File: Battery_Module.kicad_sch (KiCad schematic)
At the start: 7 parts, among them Q701 FS8205A, U701 DW01A

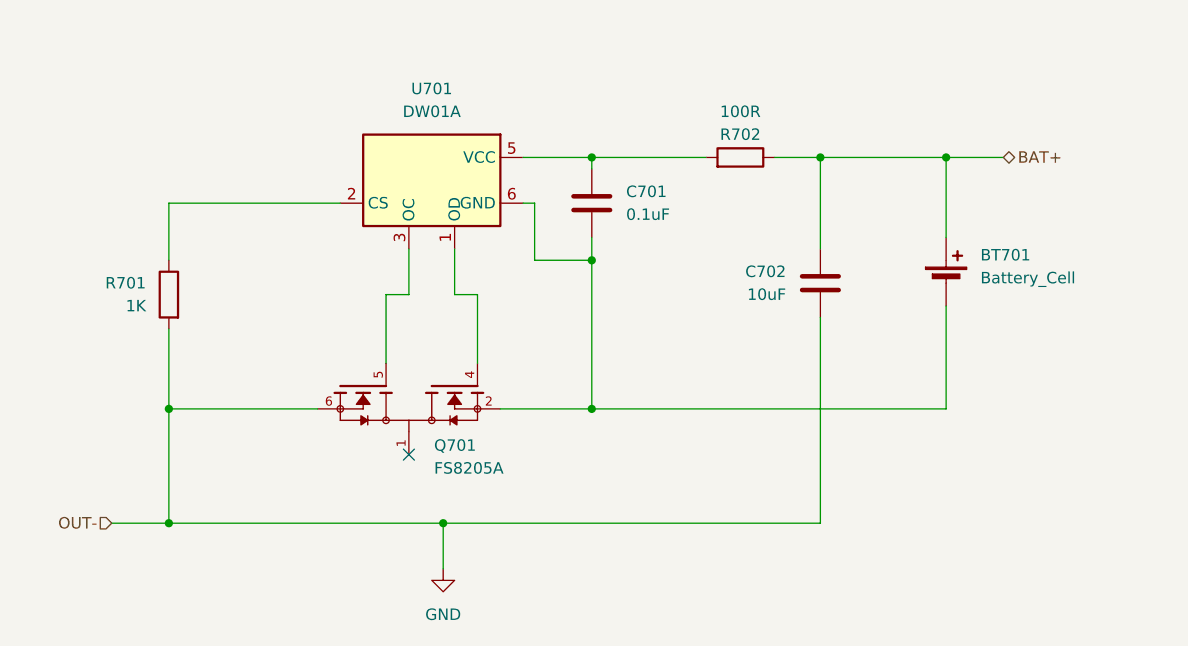
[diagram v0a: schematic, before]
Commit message: "3.3V buck boost converter added. few footprints added"
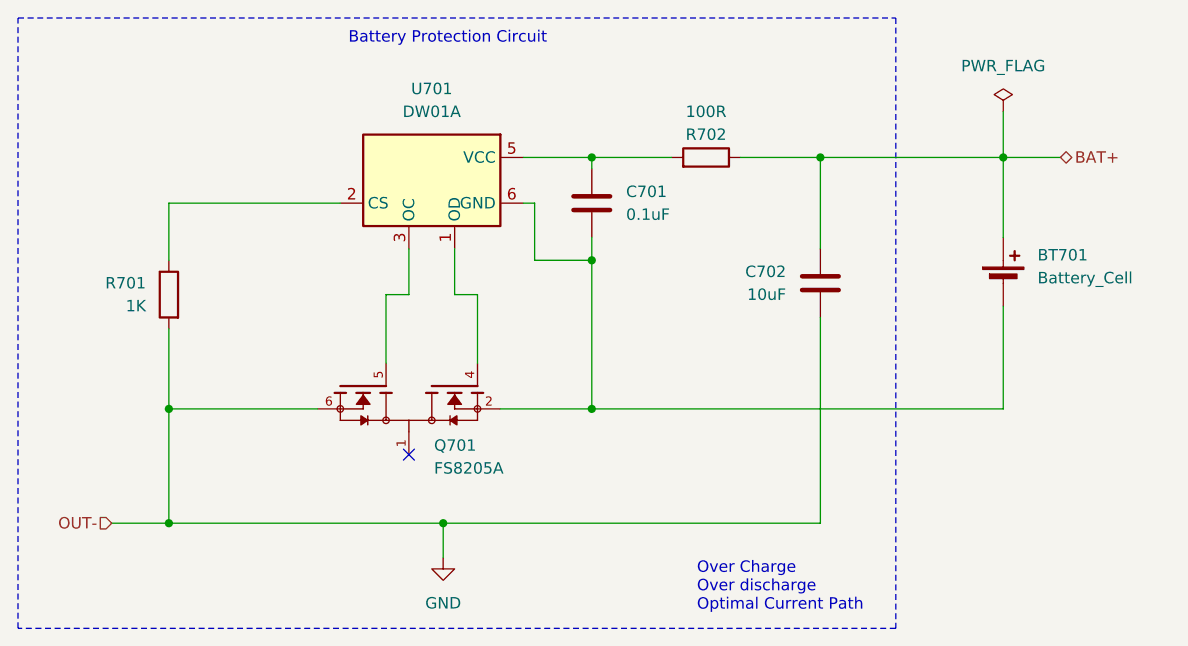
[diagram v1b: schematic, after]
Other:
- note added: "Battery Protection Circuit"
- note added: "Over Charge Over discharge Optimal Current Path"
- moved on the sheet: BT701, R702
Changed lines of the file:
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@@
 	(generator_version "9.0")
 	(paper "A4")
+	(rectangle
+		(start 83.566 72.136)
+		(end 181.102 139.954)
+		(stroke
+			(width 0)
+			(type dash)
+		)
+		(fill
+			(type none)
+		)
+	)
+	(text "Over Charge\nOver discharge\nOptimal Current Path"
+		(exclude_from_sim no)
+		(at 159.004 135.382 0)
+		(effects
+			(font
+				(size 1.27 1.27)
+			)
+			(justify left)
+		)
+	)
+	(text "Battery Protection Circuit"
+		(exclude_from_sim no)
+		(at 131.318 74.422 0)
+		(effects
+			(font
+				(size 1.27 1.27)
+			)
+		)
+	)
 	(junction
 		(at 172.72 87.63)
@@
 	)
 	(junction
-		(at 186.69 87.63)
+		(at 193.04 87.63)
 		(diameter 0)
 		(color 0 0 0 0)
@@
 	(wire
 		(pts
-			(xy 167.64 87.63) (xy 172.72 87.63)
+			(xy 163.83 87.63) (xy 172.72 87.63)
 		)
 		(stroke
@@
 	(wire
 		(pts
-			(xy 186.69 87.63) (xy 186.69 96.52)
+			(xy 193.04 87.63) (xy 193.04 96.52)
 		)
 		(stroke
@@
 	(wire
 		(pts
-			(xy 172.72 87.63) (xy 186.69 87.63)
-		)
-		(stroke
-			(width 0)
-			(type default)
-		)
-	)
-	(wire
-		(pts
-			(xy 130.81 128.27) (xy 130.81 133.35)
+			(xy 172.72 87.63) (xy 193.04 87.63)
+		)
+		(stroke
+			(width 0)
+			(type default)
+		)
+	)
+	(wire
+		(pts
+			(xy 130.81 128.27) (xy 130.81 132.08)
 		)
 		(stroke
@@
 	(wire
 		(pts
+			(xy 193.04 82.55) (xy 193.04 87.63)
+		)
+		(stroke
+			(width 0)
+			(type default)
+		)
+	)
+	(wire
+		(pts
 			(xy 127 97.79) (xy 127 102.87)
 		)
@@
 	(wire
 		(pts
-			(xy 160.02 87.63) (xy 147.32 87.63)
-		)
-		(stroke
-			(width 0)
-			(type default)
-		)
-	)
-	(wire
-		(pts
-			(xy 186.69 87.63) (xy 193.04 87.63)
-		)
-		(stroke
-			(width 0)
-			(type default)
-		)
-	)
-	(wire
-		(pts
-			(xy 147.32 115.57) (xy 186.69 115.57)
+			(xy 156.21 87.63) (xy 147.32 87.63)
+		)
+		(stroke
+			(width 0)
+			(type default)
+		)
+	)
+	(wire
+		(pts
+			(xy 193.04 87.63) (xy 199.39 87.63)
+		)
+		(stroke
+			(width 0)
+			(type default)
+		)
+	)
+	(wire
+		(pts
+			(xy 147.32 115.57) (xy 193.04 115.57)
 		)
 		(stroke
@@
 	(wire
 		(pts
-			(xy 186.69 104.14) (xy 186.69 115.57)
+			(xy 193.04 104.14) (xy 193.04 115.57)
 		)
 		(stroke
@@
 	(hierarchical_label "BAT+"
 		(shape bidirectional)
-		(at 193.04 87.63 0)
+		(at 199.39 87.63 0)
 		(effects
 			(font
@@
 	(symbol
 		(lib_id "Device:R")
-		(at 163.83 87.63 270)
+		(at 160.02 87.63 270)
 		(mirror x)
 		(unit 1)
@@
 		(dnp no)
 		(property "Reference" "R702"
-			(at 163.83 85.09 90)
+			(at 160.02 85.09 90)
 			(effects
 				(font
@@
 		)
 		(property "Value" "100R"
-			(at 163.83 82.55 90)
+			(at 160.02 82.55 90)
 			(effects
 				(font
@@
 		)
 		(property "Footprint" ""
-			(at 163.83 89.408 90)
+			(at 160.02 89.408 90)
 			(effects
 				(font
@@
 		)
 		(property "Datasheet" "~"
-			(at 163.83 87.63 0)
+			(at 160.02 87.63 0)
 			(effects
 				(font
@@
 		)
 		(property "Description" "Resistor"
-			(at 163.83 87.63 0)
+			(at 160.02 87.63 0)
 			(effects
 				(font
@@
 	(symbol
 		(lib_id "power:GND")
-		(at 130.81 133.35 0)
+		(at 130.81 132.08 0)
 		(unit 1)
 		(exclude_from_sim no)
@@
 		(fields_autoplaced yes)
 		(property "Reference" "#PWR0702"
-			(at 130.81 139.7 0)
+			(at 130.81 138.43 0)
 			(effects
 				(font
@@
 		)
 		(property "Value" "GND"
-			(at 130.81 138.43 0)
+			(at 130.81 137.16 0)
 			(effects
 				(font
@@
 		)
 		(property "Footprint" ""
-			(at 130.81 133.35 0)
+			(at 130.81 132.08 0)
 			(effects
 				(font
@@
 		)
 		(property "Datasheet" ""
-			(at 130.81 133.35 0)
+			(at 130.81 132.08 0)
 			(effects
 				(font
@@
 		)
 		(property "Description" "Power symbol creates a global label with name \"GND\" , ground"
-			(at 130.81 133.35 0)
+			(at 130.81 132.08 0)
 			(effects
 				(font
@@
 	(symbol
 		(lib_id "Device:Battery_Cell")
-		(at 186.69 101.6 0)
+		(at 193.04 101.6 0)
 		(unit 1)
 		(exclude_from_sim no)
@@
 		(fields_autoplaced yes)
 		(property "Reference" "BT701"
-			(at 190.5 98.4884 0)
+			(at 196.85 98.4884 0)
 			(effects
 				(font
@@
 		)
 		(property "Value" "Battery_Cell"
-			(at 190.5 101.0284 0)
+			(at 196.85 101.0284 0)
 			(effects
 				(font
@@
 		)
 		(property "Footprint" "govi_v3_SHT41_sensor_kicad:BAT_1042P"
-			(at 186.69 100.076 90)
+			(at 193.04 100.076 90)
 			(effects
 				(font
@@
 		)
 		(property "Datasheet" "~"
-			(at 186.69 100.076 90)
+			(at 193.04 100.076 90)
 			(effects
 				(font
@@
 		)
 		(property "Description" "Single-cell battery"
-			(at 186.69 101.6 0)
+			(at 193.04 101.6 0)
 			(effects
 				(font
@@
 					(unit 1)
 				)
+			)
+		)
+	)
+	(symbol
+		(lib_id "power:PWR_FLAG")
+		(at 193.04 82.55 0)
+		(unit 1)
+		(exclude_from_sim no)
+		(in_bom yes)
+		(on_board yes)
+		(dnp no)
+		(fields_autoplaced yes)
+		(property "Reference" "#FLG0701"
+			(at 193.04 80.645 0)
+			(effects
+				(font
+					(size 1.27 1.27)
+				)
+				(hide yes)
+			)
+		)
+		(property "Value" "PWR_FLAG"
+			(at 193.04 77.47 0)
+			(effects
+				(font
+					(size 1.27 1.27)
+				)
+			)
+		)
+		(property "Footprint" ""
+			(at 193.04 82.55 0)
+			(effects
+				(font
+					(size 1.27 1.27)
+				)
+				(hide yes)
+			)
+		)
+		(property "Datasheet" "~"
+			(at 193.04 82.55 0)
+			(effects
+				(font
+					(size 1.27 1.27)
+				)
+				(hide yes)
+			)
+		)
+		(property "Description" "Special symbol for telling ERC where power comes from"
+			(at 193.04 82.55 0)
+			(effects
+				(font
+					(size 1.27 1.27)
+				)
+				(hide yes)
+			)
+		)
+		(pin "1"
+		)
+		(instances
+			(project "govi_v3_SHT41_sensor_kicad"
+				(path "/ba95ddf4-72c6-4eeb-9c09-ae7c8e5af670/625f4f9c-da9a-4f02-8306-7d03107693c0"
+					(reference "#FLG0701")
+					(unit 1)
+				)

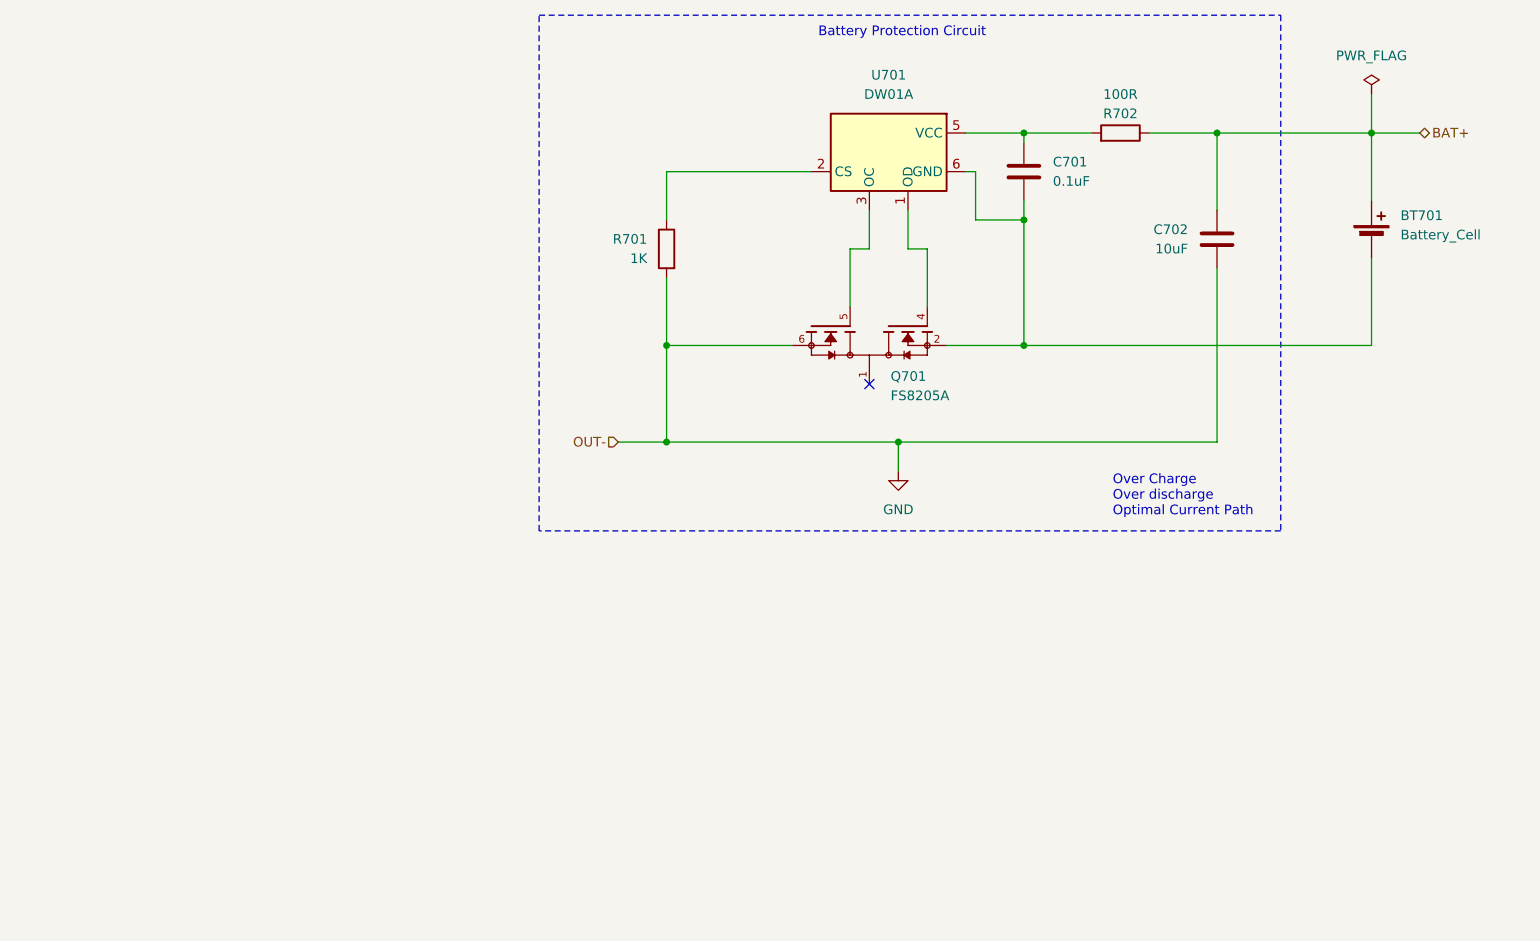
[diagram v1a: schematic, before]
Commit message: "Assign Footprints Done"
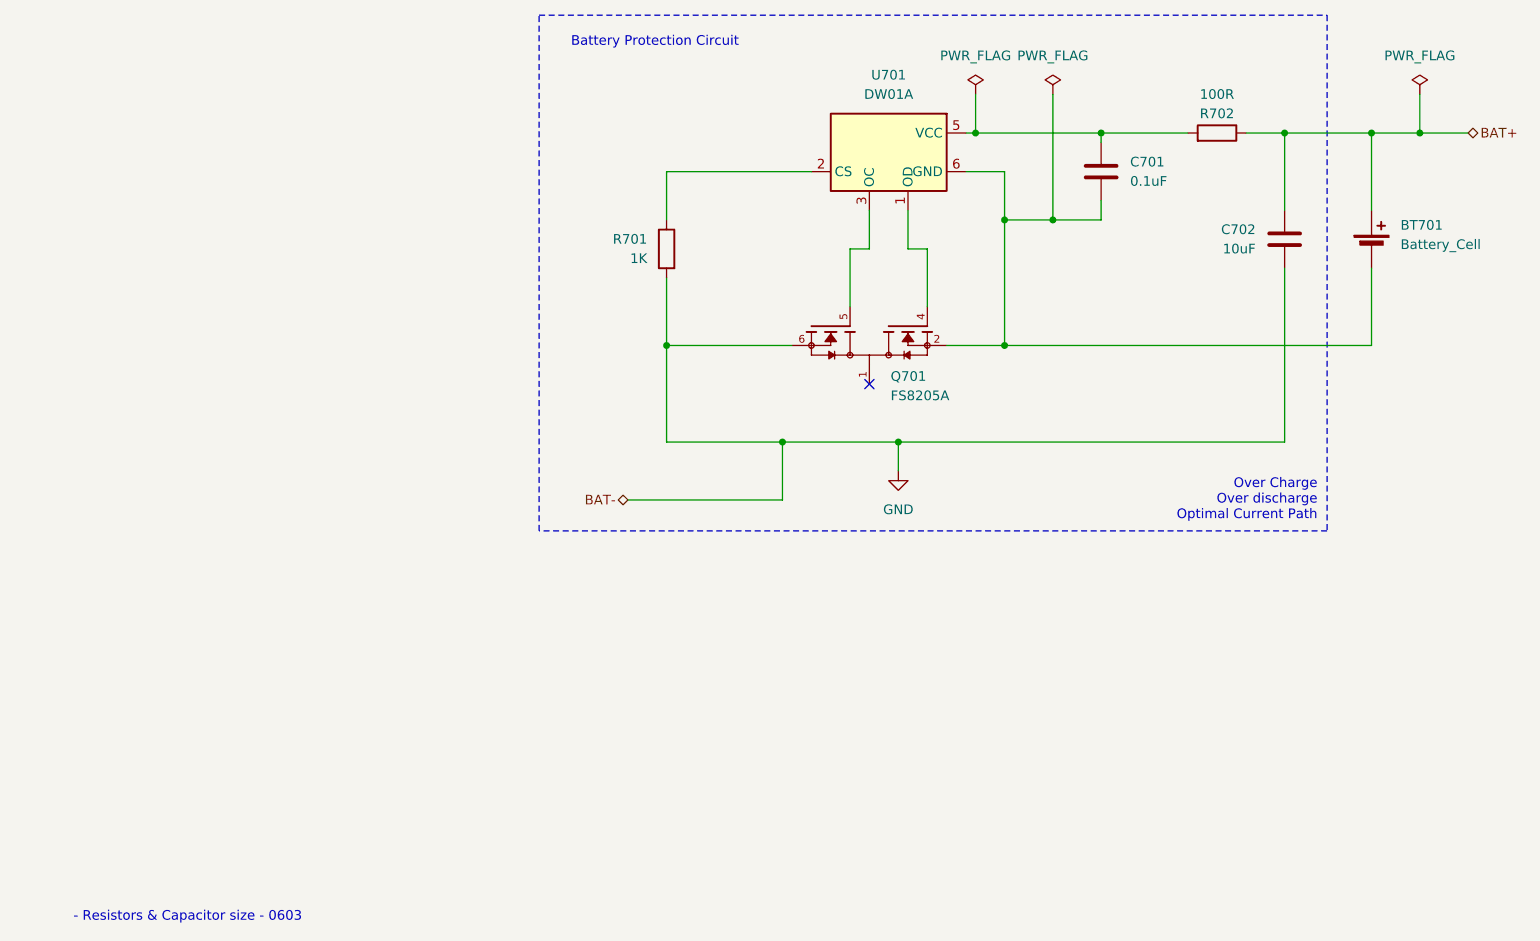
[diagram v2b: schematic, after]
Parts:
- C701, C702: footprint (none) -> Capacitor_SMD:C_0603_1608Metric_Pad1.08x0.95mm_HandSolder
- R701, R702: footprint (none) -> Resistor_SMD:R_0603_1608Metric_Pad0.98x0.95mm_HandSolder
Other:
- note added: "- Resistors & Capacitor size - 0603"
- moved on the sheet: BT701, C701, C702, R702

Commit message: "PCB front Layer Component assembly done"
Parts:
- added TP701: BAT-, TestPoint:TestPoint_Pad_D1.0mm, symbol Connector:TestPoint
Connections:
- net GND: now also TP701.1
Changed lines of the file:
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@@
+	)
+	(junction
+		(at 104.14 115.57)
+		(diameter 0)
+		(color 0 0 0 0)
 	)
 	(junction
@@
 	(wire
 		(pts
+			(xy 104.14 115.57) (xy 116.84 115.57)
+		)
+		(stroke
+			(width 0)
+			(type default)
+		)
+	)
+	(wire
+		(pts
 			(xy 132.08 102.87) (xy 134.62 102.87)
 		)
@@
 	(wire
 		(pts
+			(xy 104.14 114.3) (xy 104.14 115.57)
+		)
+		(stroke
+			(width 0)
+			(type default)
+		)
+	)
+	(wire
+		(pts
 			(xy 140.97 87.63) (xy 157.48 87.63)
 		)
@@
 	(wire
 		(pts
-			(xy 100.33 115.57) (xy 116.84 115.57)
+			(xy 100.33 115.57) (xy 104.14 115.57)
 		)
 		(stroke
@@
 					(unit 1)
 				)
+			)
+		)
+	)
+	(symbol
+		(lib_id "Connector:TestPoint")
+		(at 104.14 114.3 0)
+		(unit 1)
+		(exclude_from_sim no)
+		(in_bom yes)
+		(on_board yes)
+		(dnp no)
+		(fields_autoplaced yes)
+		(property "Reference" "TP701"
+			(at 106.68 109.7279 0)
+			(effects
+				(font
+					(size 1.27 1.27)
+				)
+				(justify left)
+			)
+		)
+		(property "Value" "BAT-"
+			(at 106.68 112.2679 0)
+			(effects
+				(font
+					(size 1.27 1.27)
+				)
+				(justify left)
+			)
+		)
+		(property "Footprint" "TestPoint:TestPoint_Pad_D1.0mm"
+			(at 109.22 114.3 0)
+			(effects
+				(font
+					(size 1.27 1.27)
+				)
+				(hide yes)
+			)
+		)
+		(property "Datasheet" "~"
+			(at 109.22 114.3 0)
+			(effects
+				(font
+					(size 1.27 1.27)
+				)
+				(hide yes)
+			)
+		)
+		(property "Description" "test point"
+			(at 104.14 114.3 0)
+			(effects
+				(font
+					(size 1.27 1.27)
+				)
+				(hide yes)
+			)
+		)
+		(pin "1"
+		)
+		(instances
+			(project ""
+				(path "/ba95ddf4-72c6-4eeb-9c09-ae7c8e5af670/625f4f9c-da9a-4f02-8306-7d03107693c0"
+					(reference "TP701")
+					(unit 1)
+				)

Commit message: "Before changing the orientation of the LoRa module. removing existing LoRa module routing."
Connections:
- net GND renamed BAT-
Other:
- moved on the sheet: TP701
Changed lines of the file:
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@@
+	)
+	(junction
+		(at 110.49 115.57)
+		(diameter 0)
+		(color 0 0 0 0)
 	)
 	(junction
@@
 	)
 	(junction
-		(at 104.14 115.57)
-		(diameter 0)
-		(color 0 0 0 0)
-	)
-	(junction
 		(at 140.97 87.63)
 		(diameter 0)
@@
 	(junction
 		(at 181.61 87.63)
-		(diameter 0)
-		(color 0 0 0 0)
-	)
-	(junction
-		(at 130.81 128.27)
 		(diameter 0)
 		(color 0 0 0 0)
@@
 	(wire
 		(pts
-			(xy 104.14 115.57) (xy 116.84 115.57)
+			(xy 110.49 110.49) (xy 110.49 115.57)
 		)
 		(stroke
@@
 	(wire
 		(pts
-			(xy 130.81 128.27) (xy 181.61 128.27)
-		)
-		(stroke
-			(width 0)
-			(type default)
-		)
-	)
-	(wire
-		(pts
-			(xy 130.81 128.27) (xy 130.81 132.08)
+			(xy 115.57 128.27) (xy 181.61 128.27)
 		)
 		(stroke
@@
 	(wire
 		(pts
-			(xy 104.14 114.3) (xy 104.14 115.57)
-		)
-		(stroke
-			(width 0)
-			(type default)
-		)
-	)
-	(wire
-		(pts
 			(xy 140.97 87.63) (xy 157.48 87.63)
 		)
@@
 	(wire
 		(pts
+			(xy 110.49 115.57) (xy 116.84 115.57)
+		)
+		(stroke
+			(width 0)
+			(type default)
+		)
+	)
+	(wire
+		(pts
 			(xy 181.61 87.63) (xy 193.04 87.63)
 		)
@@
 	(wire
 		(pts
-			(xy 100.33 115.57) (xy 104.14 115.57)
-		)
-		(stroke
-			(width 0)
-			(type default)
-		)
-	)
-	(wire
-		(pts
-			(xy 115.57 128.27) (xy 130.81 128.27)
+			(xy 100.33 115.57) (xy 110.49 115.57)
 		)
 		(stroke
@@
 	)
 	(symbol
-		(lib_id "power:GND")
-		(at 130.81 132.08 0)
-		(unit 1)
-		(exclude_from_sim no)
-		(in_bom yes)
-		(on_board yes)
-		(dnp no)
-		(fields_autoplaced yes)
-		(property "Reference" "#PWR0701"
-			(at 130.81 138.43 0)
-			(effects
-				(font
-					(size 1.27 1.27)
-				)
-				(hide yes)
-			)
-		)
-		(property "Value" "GND"
-			(at 130.81 137.16 0)
-			(effects
-				(font
-					(size 1.27 1.27)
-				)
-			)
-		)
-		(property "Footprint" ""
-			(at 130.81 132.08 0)
-			(effects
-				(font
-					(size 1.27 1.27)
-				)
-				(hide yes)
-			)
-		)
-		(property "Datasheet" ""
-			(at 130.81 132.08 0)
-			(effects
-				(font
-					(size 1.27 1.27)
-				)
-				(hide yes)
-			)
-		)
-		(property "Description" "Power symbol creates a global label with name \"GND\" , ground"
-			(at 130.81 132.08 0)
-			(effects
-				(font
-					(size 1.27 1.27)
-				)
-				(hide yes)
-			)
-		)
-		(pin "1"
-		)
-		(instances
-			(project "govi_v3_SHT41_sensor_kicad"
-				(path "/ba95ddf4-72c6-4eeb-9c09-ae7c8e5af670/625f4f9c-da9a-4f02-8306-7d03107693c0"
-					(reference "#PWR0701")
-					(unit 1)
-				)
-			)
-		)
-	)
-	(symbol
 		(lib_id "power:PWR_FLAG")
 		(at 199.39 82.55 0)
@@
 	(symbol
 		(lib_id "Connector:TestPoint")
-		(at 104.14 114.3 0)
+		(at 110.49 110.49 0)
 		(unit 1)
 		(exclude_from_sim no)
@@
 		(fields_autoplaced yes)
 		(property "Reference" "TP701"
-			(at 106.68 109.7279 0)
+			(at 113.03 105.9179 0)
 			(effects
 				(font
@@
 		)
 		(property "Value" "BAT-"
-			(at 106.68 112.2679 0)
+			(at 113.03 108.4579 0)
 			(effects
 				(font
@@
 		)
 		(property "Footprint" "TestPoint:TestPoint_Pad_D1.0mm"
-			(at 109.22 114.3 0)
+			(at 115.57 110.49 0)
 			(effects
 				(font
@@
 		)
 		(property "Datasheet" "~"
-			(at 109.22 114.3 0)
+			(at 115.57 110.49 0)
 			(effects
 				(font
@@
 		)
 		(property "Description" "test point"
-			(at 104.14 114.3 0)
-			(effects
-				(font
+			(at 110.49 110.49 0)
+			(effects
+				(font
